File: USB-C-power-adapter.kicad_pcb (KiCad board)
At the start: 2 copper layers, 21.1 x 40.1 mm, 1 part, among them J1 USB-C_GCT_USB4105-GF-A

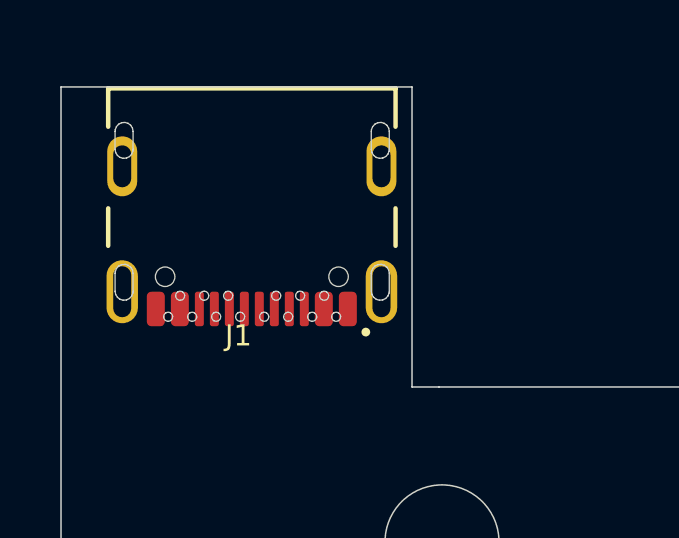
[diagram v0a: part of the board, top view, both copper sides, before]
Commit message: [#57225] Fix outline
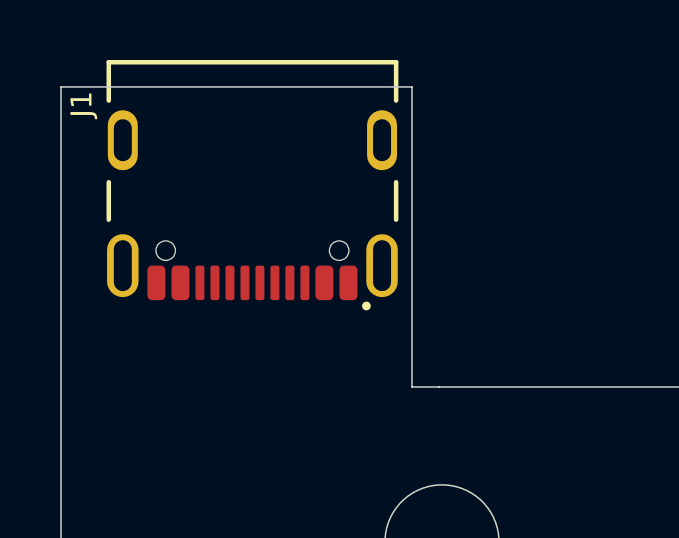
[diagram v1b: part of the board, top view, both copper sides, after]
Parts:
- moved J1 0.87 mm to (87.9, 64.1)
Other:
- outline, holes or cut-outs redrawn

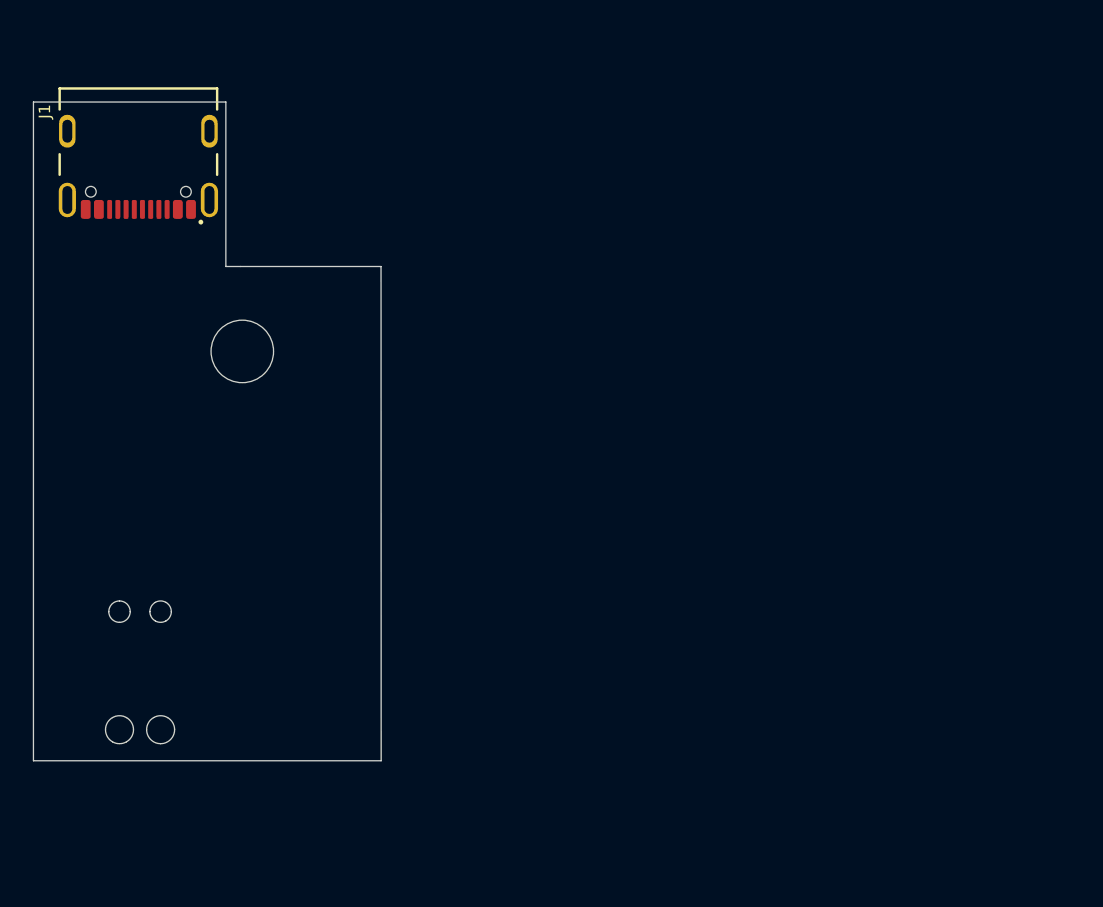
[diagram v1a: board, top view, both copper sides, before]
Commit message: [#57225] Add dimensions
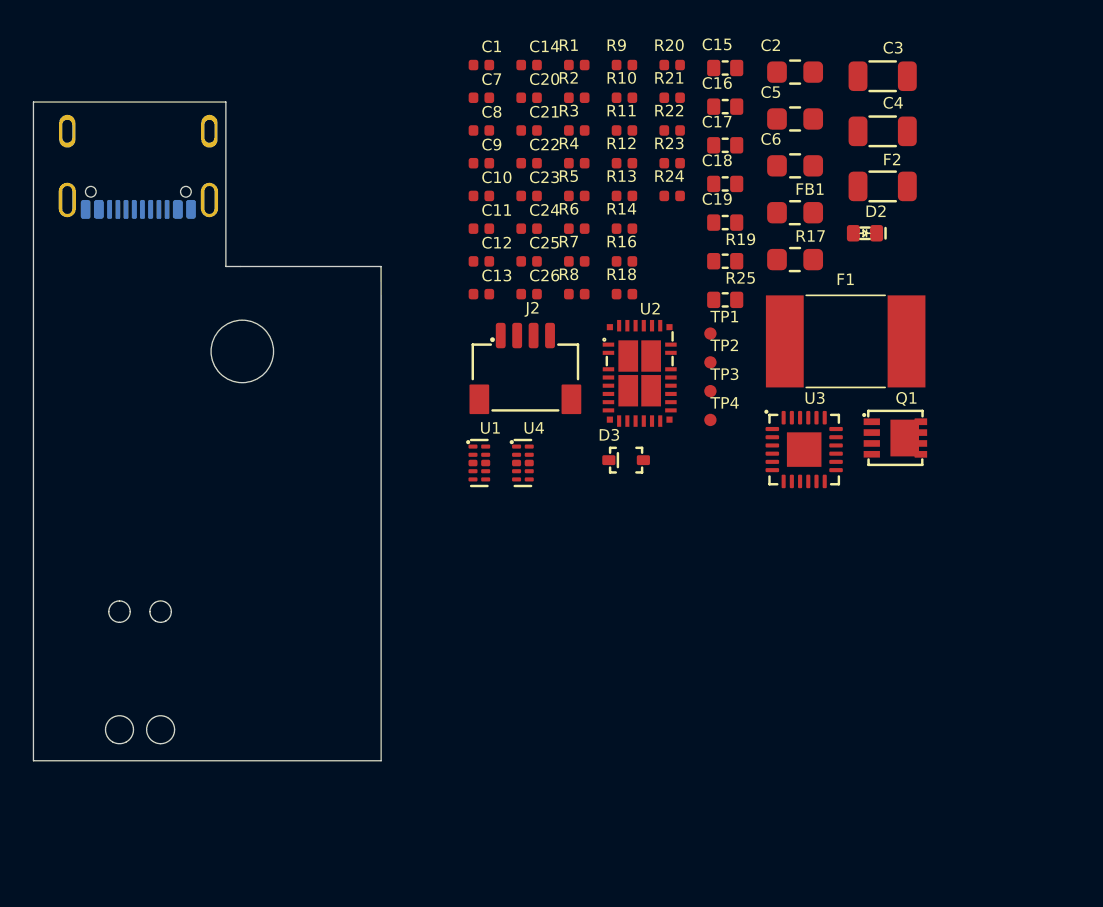
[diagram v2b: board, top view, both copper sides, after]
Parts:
- added C1: C_100n_16V_X7R_0402, antmicro-footprints:C_0402_1005Metric, F.Cu at (108.8, 58.8)
- added C10: C_1u_0402, antmicro-footprints:C_0402_1005Metric, F.Cu at (108.8, 66.8)
- added C11: C_4n7_0402, antmicro-footprints:C_0402_1005Metric, F.Cu at (108.8, 68.8)
- added C12: C_100n_0402, antmicro-footprints:C_0402_1005Metric, F.Cu at (108.8, 70.8)
- added C13: C_100n_0402, antmicro-footprints:C_0402_1005Metric, F.Cu at (108.8, 72.8)
- added C14: C_100n_0402, antmicro-footprints:C_0402_1005Metric, F.Cu at (111.7, 58.8)
- added C15: C_22u_16V_0603, antmicro-footprints:C_0603_1608Metric, F.Cu at (123.6, 59.0)
- added C16: C_22u_16V_0603, antmicro-footprints:C_0603_1608Metric, F.Cu at (123.6, 61.4)
- added C17: C_22u_16V_0603, antmicro-footprints:C_0603_1608Metric, F.Cu at (123.6, 63.7)
- added C18: C_22u_16V_0603, antmicro-footprints:C_0603_1608Metric, F.Cu at (123.6, 66.0)
- added C19: C_22u_16V_0603, antmicro-footprints:C_0603_1608Metric, F.Cu at (123.6, 68.4)
- added C2: C_10u_0805_35V, antmicro-footprints:C_0805_2012Metric, F.Cu at (127.8, 59.2)
- added C20: C_1u_0402, antmicro-footprints:C_0402_1005Metric, F.Cu at (111.7, 60.8)
- added C21: C_1u_0402, antmicro-footprints:C_0402_1005Metric, F.Cu at (111.7, 62.8)
- added C22: C_1u_0402, antmicro-footprints:C_0402_1005Metric, F.Cu at (111.7, 64.8)
- added C23: C_100n_0402, antmicro-footprints:C_0402_1005Metric, F.Cu at (111.7, 66.8)
- added C24: C_4u7_25V_0402, antmicro-footprints:C_0402_1005Metric, F.Cu at (111.7, 68.8)
- added C25: C_100n_50V_X8L_0402, antmicro-footprints:C_0402_1005Metric, F.Cu at (111.7, 70.8)
- added C26: C_1u_0402, antmicro-footprints:C_0402_1005Metric, F.Cu at (111.7, 72.8)
- added C3: C_22u_1206_35V, antmicro-footprints:C_1206_3216Metric, F.Cu at (133.2, 59.5)
- added C4: C_22u_1206_35V, antmicro-footprints:C_1206_3216Metric, F.Cu at (133.2, 62.9)
- added C5: C_10u_0805_35V, antmicro-footprints:C_0805_2012Metric, F.Cu at (127.8, 62.1)
- added C6: C_10u_0805_35V, antmicro-footprints:C_0805_2012Metric, F.Cu at (127.8, 65.0)
- added C7: C_100n_50V_X8L_0402, antmicro-footprints:C_0402_1005Metric, F.Cu at (108.8, 60.8)
- added C8: C_220n_6V3_X7R_0402, antmicro-footprints:C_0402_1005Metric, F.Cu at (108.8, 62.8)
- added C9: C_22n_0402, antmicro-footprints:C_0402_1005Metric, F.Cu at (108.8, 64.8)
- added D2: LED_G_0603_LG_L29K-G2J1-24-Z, antmicro-footprints:LED_0603_1608Metric_G, F.Cu at (132.1, 69.0)
- added D3: PMEG6002EJ,115, antmicro-footprints:D_SOD-323F, F.Cu at (117.6, 82.8)
- added F1: F_5A_2920, antmicro-footprints:2920-fuse, F.Cu at (130.9, 75.6)
- added F2: F_7A_1206, antmicro-footprints:F_1206_3216Metric, F.Cu at (133.2, 66.2)
- added FB1: FB_30Z_8.5A_Murata-BLM21SN_0805, antmicro-footprints:FB_0805_2012Metric, F.Cu at (127.8, 67.8)
- added J2: JST_SH_1x4_SM04B-SRSS-TB-LF-SN, antmicro-footprints:Conn_JST_SH_1x4_SM04B-SRSS-TB-LF-SN, F.Cu at (111.4, 77.7)
- added Q1: SQS401EN-T1_BE3, antmicro-footprints:Vishay_PowerPAK_1212-8_Single, F.Cu at (133.9, 81.5)
- added R1: R_4k7_0402, antmicro-footprints:R_0402_1005Metric, F.Cu at (114.6, 58.8)
- added R10: R_100k_0402, antmicro-footprints:R_0402_1005Metric, F.Cu at (117.5, 60.8)
- added R11: R_12k_0402, antmicro-footprints:R_0402_1005Metric, F.Cu at (117.5, 62.8)
- added R12: R_0R_0402, antmicro-footprints:R_0402_1005Metric, F.Cu at (117.5, 64.8)
- added R13: R_110k_0402, antmicro-footprints:R_0402_1005Metric, F.Cu at (117.5, 66.8)
- added R14: R_10k_0402, antmicro-footprints:R_0402_1005Metric, F.Cu at (117.5, 68.8)
- added R16: R_2k2_0402, antmicro-footprints:R_0402_1005Metric, F.Cu at (117.5, 70.8)
- added R17: R_4k7_0805, antmicro-footprints:R_0805_2012Metric, F.Cu at (127.8, 70.7)
- added R18: R_10k_0402, antmicro-footprints:R_0402_1005Metric, F.Cu at (117.5, 72.8)
- added R19: R_470R_0603, antmicro-footprints:R_0603_1608Metric, F.Cu at (123.6, 70.8)
- added R2: R_4k7_0402, antmicro-footprints:R_0402_1005Metric, F.Cu at (114.6, 60.8)
- added R20: R_0R_0402, antmicro-footprints:R_0402_1005Metric, F.Cu at (120.4, 58.8)
- added R21: R_0R_0402, antmicro-footprints:R_0402_1005Metric, F.Cu at (120.4, 60.8)
- added R22: R_100k_0402, antmicro-footprints:R_0402_1005Metric, F.Cu at (120.4, 62.8)
- added R23: R_22k_0402, antmicro-footprints:R_0402_1005Metric, F.Cu at (120.4, 64.8)
- added R24: R_100R_0402, antmicro-footprints:R_0402_1005Metric, F.Cu at (120.4, 66.8)
- added R25: R_3k9_0603, antmicro-footprints:R_0603_1608Metric, F.Cu at (123.6, 73.1)
- added R3: R_24k_0402, antmicro-footprints:R_0402_1005Metric, F.Cu at (114.6, 62.8)
- added R4: R_10k_0402, antmicro-footprints:R_0402_1005Metric, F.Cu at (114.6, 64.8)
- added R5: R_0R_0402, antmicro-footprints:R_0402_1005Metric, F.Cu at (114.6, 66.8)
- added R6: R_0R_0402, antmicro-footprints:R_0402_1005Metric, F.Cu at (114.6, 68.8)
- added R7: R_0R_0402, antmicro-footprints:R_0402_1005Metric, F.Cu at (114.6, 70.8)
- added R8: R_0R_0402, antmicro-footprints:R_0402_1005Metric, F.Cu at (114.6, 72.8)
- added R9: R_124k_0402, antmicro-footprints:R_0402_1005Metric, F.Cu at (117.5, 58.8)
- added TP1: TP_0.75mm_SMD, antmicro-footprints:TP_SMD_0.75mm, F.Cu at (122.7, 75.2)
- added TP2: TP_0.75mm_SMD, antmicro-footprints:TP_SMD_0.75mm, F.Cu at (122.7, 76.9)
- added TP3: TP_0.75mm_SMD, antmicro-footprints:TP_SMD_0.75mm, F.Cu at (122.7, 78.7)
- added TP4: TP_0.75mm_SMD, antmicro-footprints:TP_SMD_0.75mm, F.Cu at (122.7, 80.4)
- added U1: TPD4E02B04DQA, antmicro-footprints:USON-10_2.5x1mm_P0.5mm, F.Cu at (108.6, 83.0)
- added U2: LT8350RV, antmicro-footprints:QFN-32-4EP_4x6mm_P0.5mm, F.Cu at (118.4, 77.6)
- added U3: STUSB4500_QFN, antmicro-footprints:QFN-24-1EP_4x4mm_P0.5_EP2.1x2.1mm, F.Cu at (128.4, 82.2)
- added U4: TPD4E02B04DQA, antmicro-footprints:USON-10_2.5x1mm_P0.5mm, F.Cu at (111.3, 83.0)
- J1: moved to B.Cu
- turned J1 to 0 degrees

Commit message: [#57225] Add MolexNano Fit
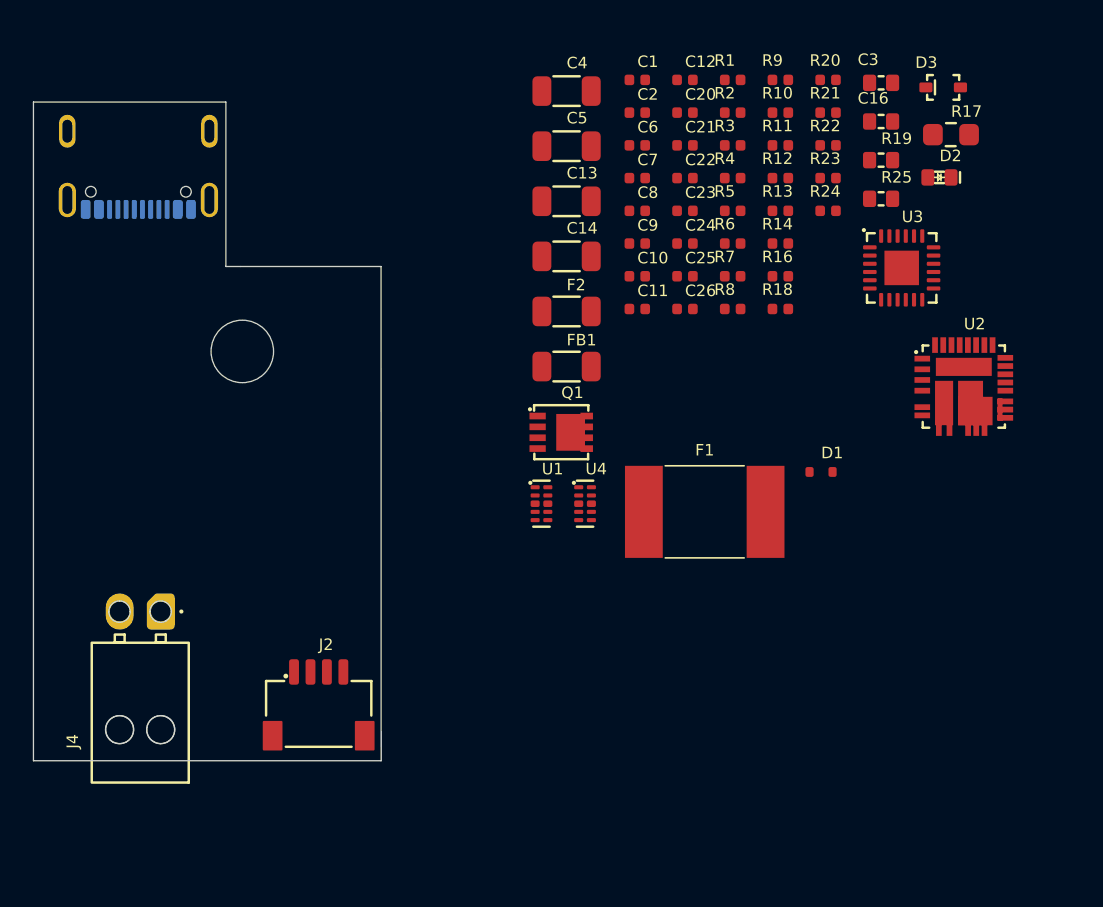
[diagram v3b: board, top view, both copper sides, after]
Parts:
- removed C15, C17, C18, C19: C_22u_16V_0603, antmicro-footprints:C_0603_1608Metric
- removed TP1, TP2, TP3, TP4: TP_0.75mm_SMD, antmicro-footprints:TP_SMD_0.75mm
- added D1: ESD5B5_0ST1G, antmicro-footprints:SOD-523_NP, F.Cu at (129.4, 83.6)
- added J4: Molex_Nano-Fit_1x2_105313-2202_Horizontal, antmicro-footprints:Conn_Molex_Nano-Fit_1x2_105313-2202_Horizontal, F.Cu at (89.3, 92.0)
- C10: value C_1u_0402 -> C_270p_25V_0402
- C11: value C_4n7_0402 -> C_1n2_50V_0402
- C13, C14: value C_100n_0402 -> C_47u_16V_1206; footprint antmicro-footprints:C_0402_1005Metric -> antmicro-footprints:C_1206_3216Metric
- C16: value C_22u_16V_0603 -> C_10u_25V_0603
- C2: value C_10u_0805_35V -> C_1u_0402; footprint antmicro-footprints:C_0805_2012Metric -> antmicro-footprints:C_0402_1005Metric
- C3: value C_22u_1206_35V -> C_4u7_0603; footprint antmicro-footprints:C_1206_3216Metric -> antmicro-footprints:C_0603_1608Metric
- C4: value C_22u_1206_35V -> C_10u_1206_50V
- C5: value C_10u_0805_35V -> C_10u_1206_50V; footprint antmicro-footprints:C_0805_2012Metric -> antmicro-footprints:C_1206_3216Metric
- C6: value C_10u_0805_35V -> C_33n_0402; footprint antmicro-footprints:C_0805_2012Metric -> antmicro-footprints:C_0402_1005Metric
- C7: value C_100n_50V_X8L_0402 -> C_100n_50V_0402
- C8: value C_220n_6V3_X7R_0402 -> C_100n_0402
- C9: value C_22n_0402 -> C_1n2_50V_0402
- FB1: value FB_30Z_8.5A_Murata-BLM21SN_0805 -> FB_10Z_10A_1206; footprint antmicro-footprints:FB_0805_2012Metric -> antmicro-footprints:FB_1206_3216Metric
- R10: value R_100k_0402 -> R_3R3_0402
- R11: value R_12k_0402 -> R_8k66_0402
- R12: value R_0R_0402 -> R_316k_0402
- R13: value R_110k_0402 -> R_140k_0.1%_0402
- R14: value R_10k_0402 -> R_10k_0.1%_0402
- R3: value R_24k_0402 -> R_2k_0402
- R4: value R_10k_0402 -> R_0R_0402
- R5: value R_0R_0402 -> R_60k4_0402
- R6: value R_0R_0402 -> R_100k_0402
- R7: value R_0R_0402 -> R_26k7_0402
- R9: value R_124k_0402 -> R_100k_0402
- U2: value LT8350RV -> SIC477ED-T1-GE3; footprint antmicro-footprints:QFN-32-4EP_4x6mm_P0.5mm -> antmicro-footprints:SIC47XED-T1-GE3
- moved D3 29.8 mm to (136.8, 60.2)
- moved J2 24.0 mm to (98.9, 98.2)
- moved F2 20.7 mm to (113.9, 73.8)
- moved Q1 20.3 mm to (113.6, 81.2)
- moved U2 19.7 mm to (138.1, 78.4)
- moved C4 19.4 mm to (113.9, 60.4)
- moved FB1 16.8 mm to (113.9, 77.2)
- moved C12 16.6 mm to (121.1, 59.7)
- moved C5 14.0 mm to (113.9, 63.8)
- moved F1 13.4 mm to (122.3, 86.0)
- moved U3 12.5 mm to (134.3, 71.2)
- moved R17 12.1 mm to (137.3, 63.1)
- moved C14 11.9 mm to (113.9, 70.5)
- moved R19 11.3 mm to (133.1, 64.6)
- moved R25 11.3 mm to (133.1, 67.0)
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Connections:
- C10 pad 1: GND -> Net-(C10-Pad1)
- C10 pad 2: Net-(U2-INTVCC) -> GND
- C11 pad 1: GND -> /12V_SNS
- C11 pad 2: Net-(C11-Pad2) -> 12V0
- C12 pad 1: Net-(U2-BST1) -> 12V0
- C12 pad 2: Net-(C12-Pad2) -> GND
- C13 pad 1: Net-(U2-BST2) -> GND
- C13 pad 2: Net-(C13-Pad2) -> 12V0
- C14 pad 2: /IS.P -> 12V0
- C16 pad 2: /IS.P -> 12V0
- C2 pad 1: GND -> /VDD_12V_DCDC
- C2 pad 2: VCC -> GND
- C3 pad 1: GND -> /VDRV_12V_DCDC
- C3 pad 2: Net-(C3-Pad2) -> GND
- C4 pad 1: GND -> Net-(U2-V_{CIN})
- C4 pad 2: Net-(C3-Pad2) -> GND
- C5 pad 1: GND -> Net-(U2-V_{CIN})
- C5 pad 2: Net-(C3-Pad2) -> GND
- C6 pad 1: GND -> /12V_SS
- C6 pad 2: Net-(C3-Pad2) -> GND
- C7 pad 1: GND -> Net-(U2-V_{CIN})
- C7 pad 2: Net-(C3-Pad2) -> GND
- C8 pad 1: GND -> Net-(C8-Pad1)
- C8 pad 2: Net-(U2-VREF) -> Net-(U2-BOOT)
- C9 pad 1: GND -> Net-(U2-V_{SNS})
- C9 pad 2: Net-(U2-SS) -> /12V_SNS
- FB1 pad 2: Net-(C3-Pad2) -> Net-(U2-V_{CIN})
- R10 pad 1: Net-(U2-INTVCC) -> Net-(C8-Pad1)
- R10 pad 2: Net-(U2-~{PGOOD}) -> Net-(R10-Pad2)
- R11 pad 1: Net-(C11-Pad2) -> Net-(L1-Pad1)
- R11 pad 2: Net-(U2-VC) -> /12V_SNS
- R12 pad 2: /IS.P -> Net-(C10-Pad1)
- R13 pad 1: Net-(U2-FB) -> Net-(U2-V_{FB})
- R13 pad 2: /IS.P -> 12V0
- R14 pad 2: Net-(U2-FB) -> Net-(U2-V_{FB})
- R3 pad 1: Net-(U2-EN/UVLO) -> /12V_MODE
- R3 pad 2: Net-(C3-Pad2) -> GND
- R4 pad 1: GND -> /VDD_12V_DCDC
- R4 pad 2: Net-(U2-EN/UVLO) -> /12V_ILIM
- R5 pad 1: Net-(U2-VREF) -> /12V_ILIM
- R5 pad 2: Net-(U2-LOADEN) -> GND
- R6 pad 1: Net-(U2-VREF) -> Net-(U2-EN)
- R6 pad 2: Net-(U2-CTRL) -> Net-(U2-V_{CIN})
- R7 pad 1: Net-(U2-VREF) -> /12V_FSW
- R7 pad 2: Net-(U2-SYNC/MODE) -> GND
- R8 pad 1: GND -> Net-(U2-V_{SNS})
- R8 pad 2: Net-(U2-SYNC/MODE) -> 12V0
- R9 pad 1: GND -> PWR_GOOD
- R9 pad 2: Net-(U2-RT) -> /VDD_12V_DCDC
- U2 pad 10: Net-(U2-ISMON) -> GND
- U2 pad 11: /IS.P -> GND
- U2 pad 12: +12V -> Net-(L1-Pad1)
- U2 pad 13: Net-(U2-CTRL) -> Net-(L1-Pad1)
- U2 pad 14: Net-(U2-FB) -> Net-(L1-Pad1)
- U2 pad 15: Net-(U2-VC) -> unconnected-(U2-GL-Pad15)
- U2 pad 16: Net-(U2-~{PGOOD}) -> /VDRV_12V_DCDC
- U2 pad 17: Net-(U2-SS) -> GND
- U2 pad 18: Net-(U2-RT) -> unconnected-(U2-ULTRASONIC-Pad18)
- U2 pad 19: Net-(U2-SYNC/MODE) -> /12V_SS
- U2 pad 2: Net-(C3-Pad2) -> PWR_GOOD
- U2 pad 20: Net-(U2-CLKOUT) -> Net-(U2-V_{SNS})
- U2 pad 22: Net-(U2-LOADTG) -> Net-(U2-V_{FB})
- U2 pad 24: /IS.P -> /12V_FSW
- U2 pad 25: /IS.P -> /12V_ILIM
- U2 pad 27: Net-(C13-Pad2) -> /12V_MODE
- U2 pad 28: Net-(C13-Pad2) -> GND
- U2 pad 3: Net-(C3-Pad2) -> Net-(U2-EN)
- U2 pad 5: Net-(U2-EN/UVLO) -> Net-(R10-Pad2)
- U2 pad 6: Net-(U2-INTVCC) -> Net-(R10-Pad2)
- U2 pad 7: Net-(U2-INTVCC) -> Net-(U2-V_{CIN})
- U2 pad 8: Net-(U2-LOADEN) -> Net-(U2-V_{CIN})
- U2 pad 9: Net-(U2-VREF) -> GND
